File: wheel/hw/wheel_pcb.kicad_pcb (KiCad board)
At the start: 2 copper layers, 42 x 65 mm, 54 parts, among them J1 LCD, J2 DEBUG, J3 LCD_BL, J4 CAR, SW1 CONFIG, U1 LPC11C24FBD48, U2 TPS62175, U3 TLV70233_SOT23-5, Y1 12MHz

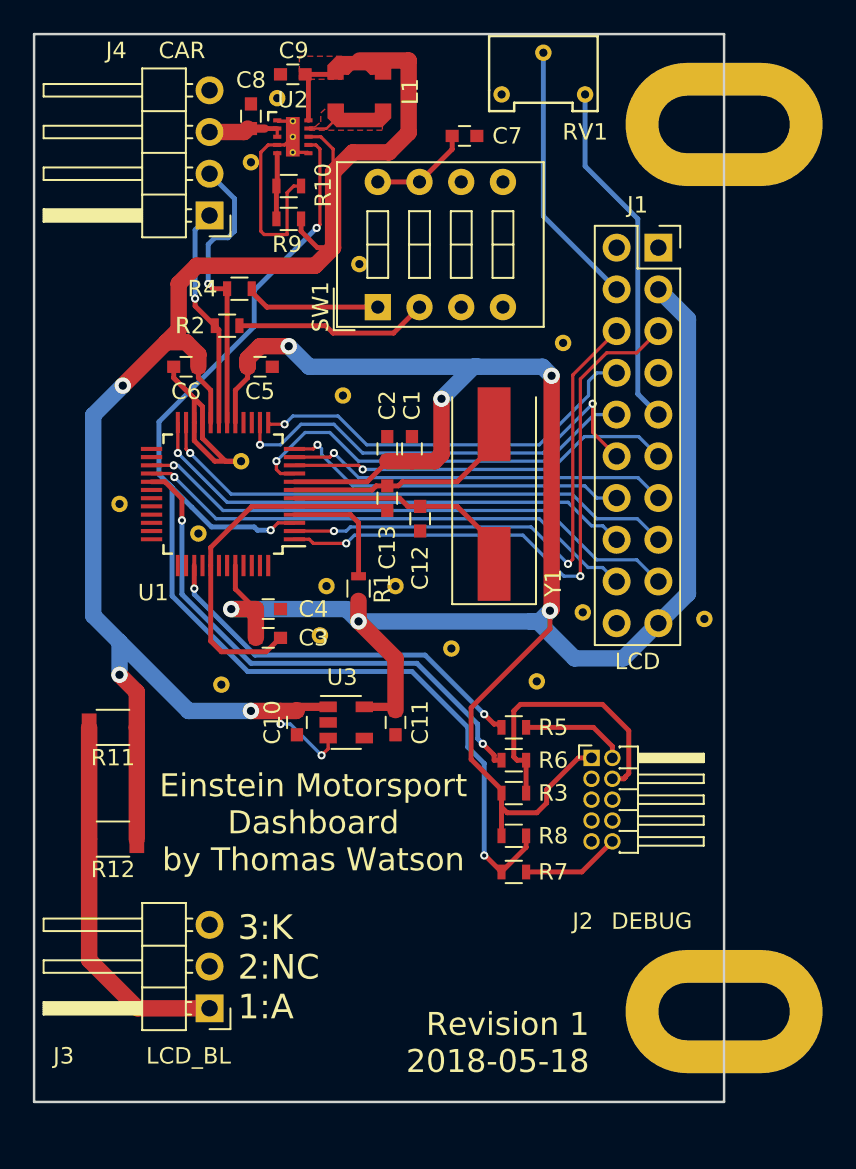
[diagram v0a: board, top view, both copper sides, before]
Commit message: remove dashboard specific parts
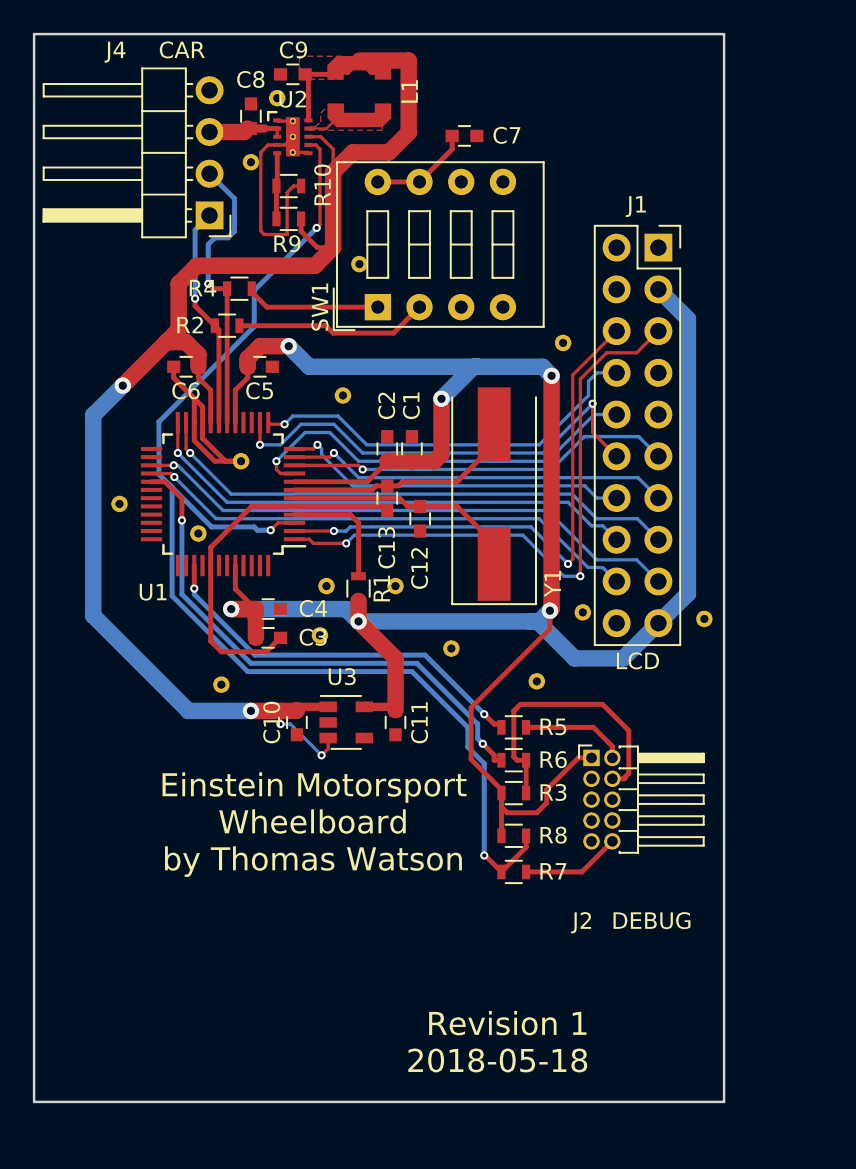
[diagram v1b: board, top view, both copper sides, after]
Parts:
- removed J3: LCD_BL, Pin_Headers:Pin_Header_Angled_1x03_Pitch2.54mm
- removed R11, R12: 36, Resistors_SMD:R_1206
- removed the REF** at (265.0, 114.5)
- removed the REF** at (265.0, 60.5)
- removed RV1: 10k, custom_footprints:Bourns_3362X
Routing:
- net /LCD_LED_A: track 22.7 -> 0.00 mm
- net /LCD_VEE: track 21.3 -> 0.00 mm
- net /LCD_V0: track 16.3 -> 0.00 mm
- net +5V: track 106.6 -> 94.1 mm, vias 5 -> 4
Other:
- board text added: "Einstein Motorsport Wheelboard by Thomas Watson"
- board text removed: "3:K 2:NC 1:A"
- board text removed: "Einstein Motorsport Dashboard by Thomas Watson"

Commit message: preliminarily lay out and pin wheel connectors
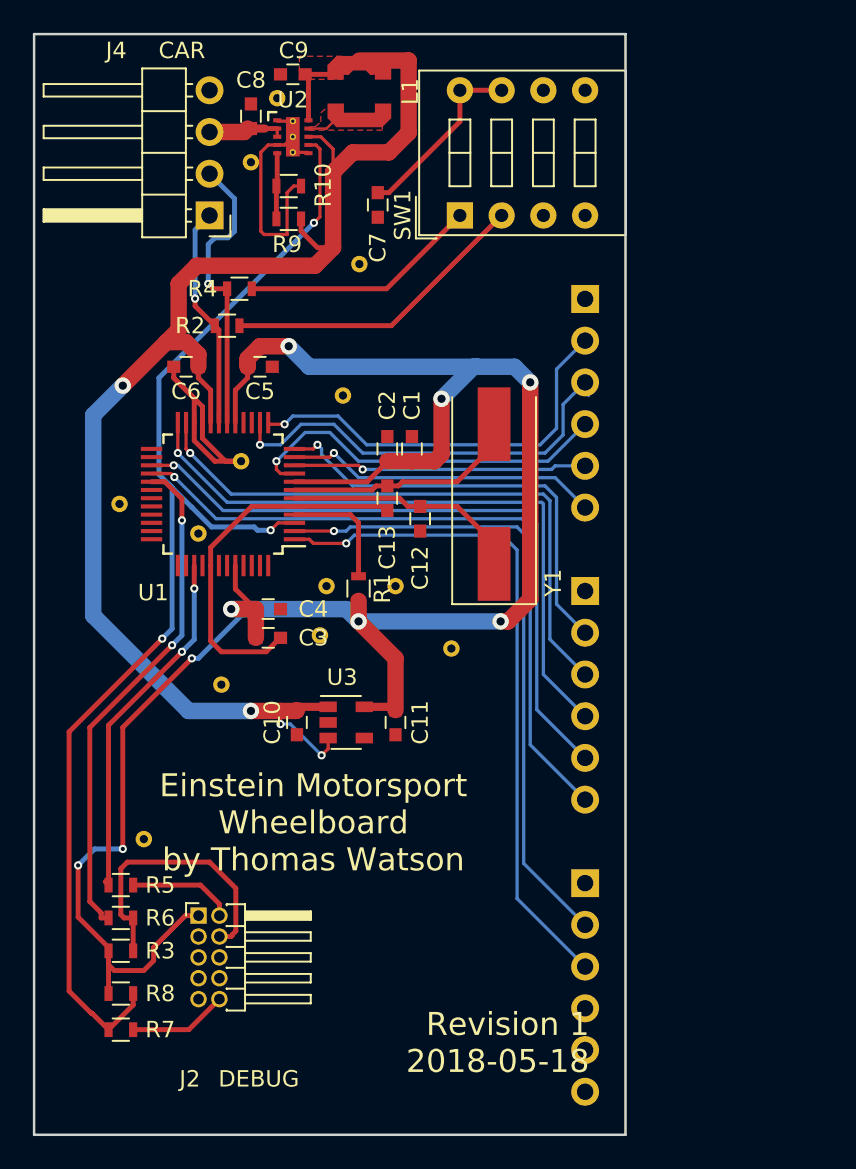
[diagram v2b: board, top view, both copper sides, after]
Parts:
- removed J1: LCD, Socket_Strips:Socket_Strip_Straight_2x10_Pitch2.54mm
- removed the REF** at (255.2, 73.8)
- removed the REF** at (263.8, 90.6)
- removed the REF** at (256.4, 90.2)
- added J3: IO_C, Pin_Headers:Pin_Header_Angled_1x06_Pitch2.54mm, B.Cu at (256.5, 71.1)
- added J5: IO_B, Pin_Headers:Pin_Header_Angled_1x06_Pitch2.54mm, B.Cu at (256.5, 88.9)
- added J6: IO_A, Pin_Headers:Pin_Header_Angled_1x06_Pitch2.54mm, B.Cu at (256.5, 106.7)
- moved J2 25.8 mm to (233.0, 108.7)
- moved R8 25.8 mm to (228.3, 113.4)
- moved R3 25.8 mm to (228.3, 110.8)
- moved R5 25.8 mm to (228.3, 106.8)
- moved R6 25.8 mm to (228.3, 108.8)
- moved R7 25.8 mm to (228.3, 115.6)
- moved REF** 25.8 mm to (229.7, 104.0)
- moved SW1 7.49 mm to (248.9, 66.0)
- moved C7 6.75 mm to (243.9, 65.4), turned to 270 degrees
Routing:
- net +3V3: track 147.1 -> 125.6 mm, vias 6 -> 9
- net /LCD_DB7: track 31.0 -> 42.4 mm
- net /LCD_DB5: track 30.7 -> 39.4 mm
- net /CANH_TERM: track 12.0 -> 18.9 mm
- net /LCD_DB6: track 33.8 -> 40.4 mm
- net /LCD_~RD: track 33.1 -> 39.6 mm, vias 2 -> 1
- net /CANL_TERM: track 8.25 -> 14.7 mm
- net /LCD_DB0: track 23.6 -> 17.9 mm
- net /LCD_DB3: track 21.3 -> 26.5 mm
- net Net-(C7-Pad1): track 6.23 -> 11.2 mm
- net /LCD_~WR: track 36.7 -> 41.3 mm, vias 2 -> 1
- net /LCD_DB2: track 23.4 -> 19.2 mm
- net /LCD_DB4: track 32.6 -> 36.5 mm
- net /LCD_~RST: track 25.0 -> 22.9 mm
- net /SWDIO: track 23.8 -> 21.9 mm
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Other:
- board size 42 x 65 mm -> 36 x 67 mm

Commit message: move connectors around to fit within constraints
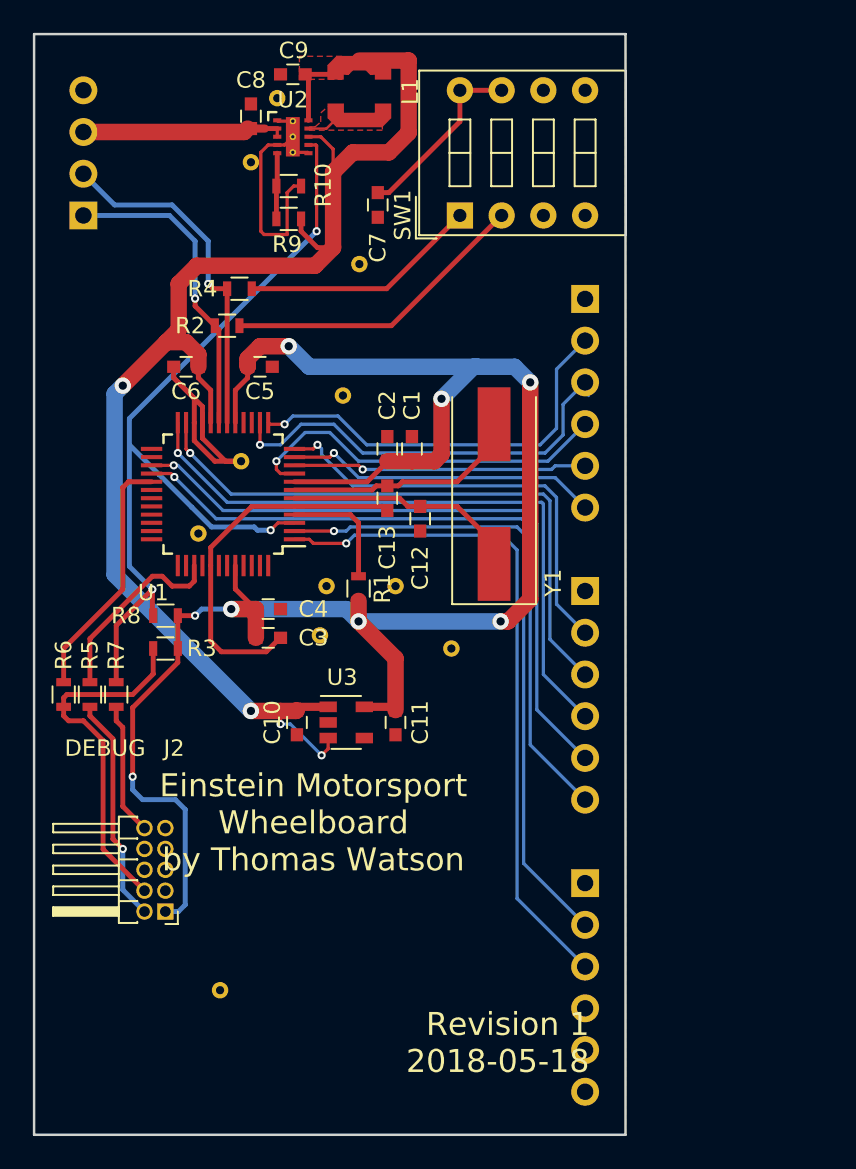
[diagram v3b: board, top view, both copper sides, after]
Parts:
- removed the REF** at (234.4, 94.6)
- removed the REF** at (228.2, 83.6)
- J4: moved to B.Cu
- moved R8 23.2 mm to (231.0, 90.4), turned to 180 degrees
- moved R7 20.4 mm to (228.0, 95.2), turned to 270 degrees
- moved R3 18.6 mm to (231.0, 92.4), turned to 180 degrees
- moved R6 14.0 mm to (224.8, 95.2), turned to 270 degrees
- moved R5 11.8 mm to (226.4, 95.2), turned to 90 degrees
- moved REF** 10.3 mm to (234.3, 113.2), turned to 180 degrees
- moved J4 7.68 mm to (226.0, 66.0), turned to 0 degrees
- moved J2 2.04 mm to (231.0, 108.4), turned to 180 degrees
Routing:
- net /MCU_~RESET: track 74.4 -> 53.4 mm
- net /SWCLK: track 30.9 -> 15.2 mm, vias 2 -> 0
- net +3V3: track 125.6 -> 113.7 mm, vias 9 -> 8
- net /SWDIO: track 21.9 -> 11.9 mm, vias 2 -> 0
- net +BATT: track 4.71 -> 12.4 mm
- net Net-(J2-Pad2): track 6.43 -> 13.8 mm, vias 0 -> 1
- net /CANH: track 13.6 -> 19.1 mm
- net Net-(J2-Pad4): track 17.2 -> 21.9 mm
- net /CANL: track 17.9 -> 21.3 mm
- net +5V: track 94.1 -> 90.8 mm
- net Net-(J2-Pad10): track 6.02 -> 8.09 mm
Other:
- board text added: "1:CANH 2:CANL 3:+12V 4:GND"
- board text removed: "4:GND 3:+12V 2:CANL 1:CANH"

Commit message: relabel i/o with less lcd names
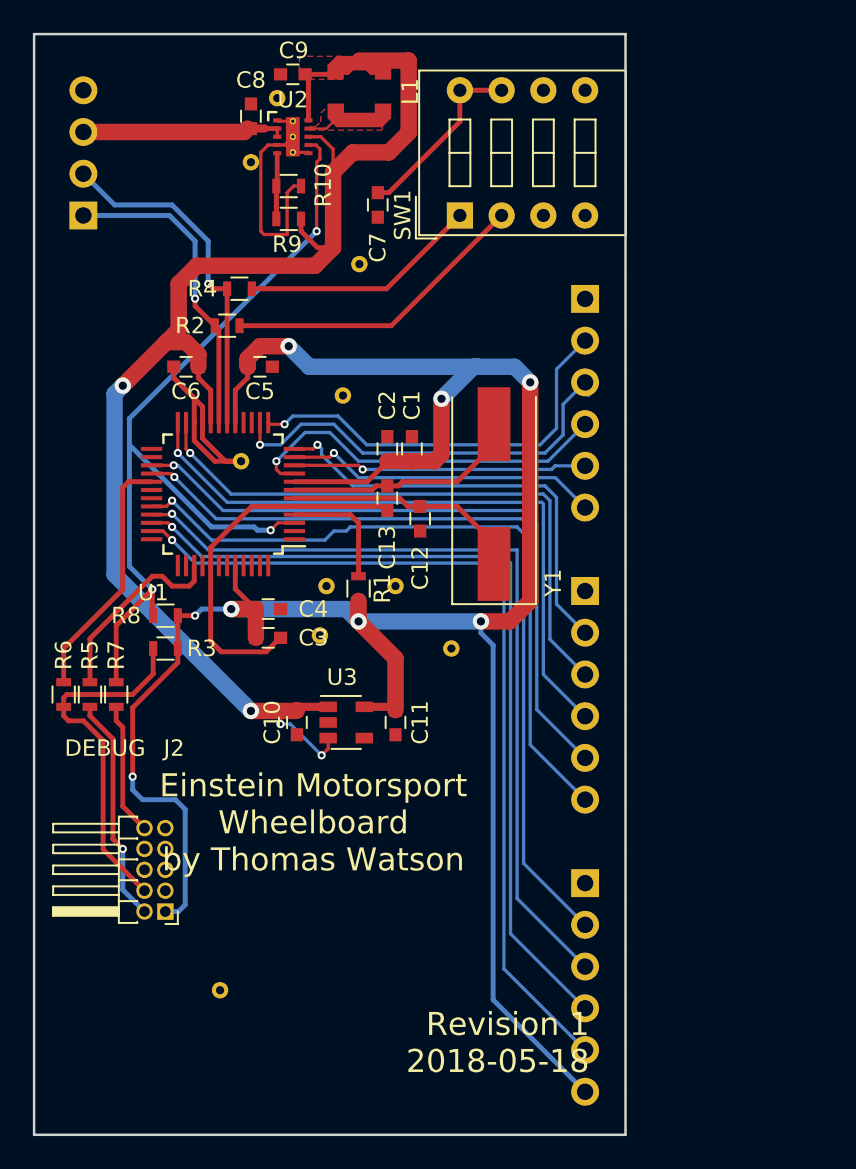
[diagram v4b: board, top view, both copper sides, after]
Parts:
- removed the REF** at (233.0, 85.4)
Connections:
- net /LCD_C/~D renamed /IO_C1
- net /LCD_DB0 renamed /IO_C4
- net /LCD_DB1 renamed /IO_C2
- net /LCD_DB2 renamed /IO_C5
- net /LCD_DB3 renamed /IO_B1
- net /LCD_DB4 renamed /IO_B2
- net /LCD_DB5 renamed /IO_B3
- net /LCD_DB6 renamed /IO_B4
- net /LCD_DB7 renamed /IO_B5
- net /LCD_~RST renamed /IO_C3
- J6 pad 2: /LCD_~RD -> /IO_A1
- J6 pad 3: /LCD_~WR -> /IO_A2
- J6 pad 4: Net-(J6-Pad4) -> /IO_A3
- J6 pad 5: Net-(J6-Pad5) -> /IO_A4
- J6 pad 6: Net-(J6-Pad6) -> +3V3
- U1 pad 1: /LCD_~WR -> Net-(U1-Pad1)
- U1 pad 2: /LCD_~RD -> Net-(U1-Pad2)
- U1 pad 32: Net-(U1-Pad32) -> /IO_A1
- U1 pad 33: Net-(U1-Pad33) -> /IO_A2
- U1 pad 34: Net-(U1-Pad34) -> /IO_A3
- U1 pad 35: Net-(U1-Pad35) -> /IO_A4
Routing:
- net /IO_A4: track 0.00 -> 53.4 mm, vias 0 -> 1
- net /IO_A3: track 0.00 -> 51.8 mm, vias 0 -> 1
- net /IO_A2: track 0.00 -> 50.3 mm, vias 0 -> 1
- net /IO_A1: track 0.00 -> 49.7 mm, vias 0 -> 1
- net /LCD_~WR: track 41.3 -> 0.00 mm, vias 1 -> 0
- net /LCD_~RD: track 39.6 -> 0.00 mm, vias 1 -> 0
- net +3V3: track 113.7 -> 145.1 mm

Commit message: clean up button bus
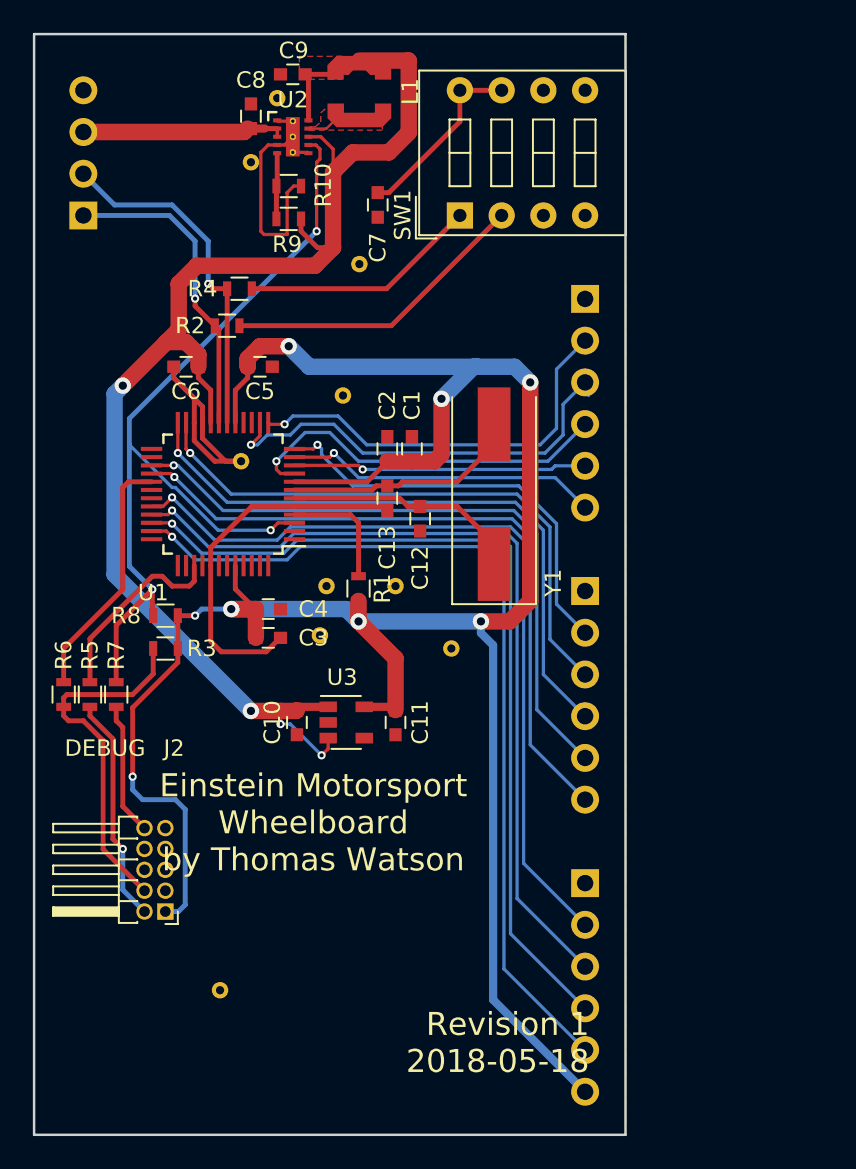
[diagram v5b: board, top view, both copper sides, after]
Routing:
- net /IO_A4: track 53.4 -> 55.1 mm
- net /IO_A3: track 51.8 -> 53.1 mm
- net /IO_A2: track 50.3 -> 51.3 mm
- net /IO_B3: track 39.4 -> 38.4 mm
- net /IO_B1: track 26.5 -> 25.6 mm
- net /IO_B2: track 36.5 -> 35.6 mm
- net /IO_C2: track 26.1 -> 26.9 mm
